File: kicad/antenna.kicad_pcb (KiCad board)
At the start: 2 copper layers, 84.1 x 61.7 mm, 37 parts, among them J1 Bus_PCI_Express_x1, J4 Conn_01x02, J5 Conn_02x08_Odd_Even, J6 USB_C_Receptacle_USB2.0_16P, U2 RP2040, U4 W25Q128JVP, U9 MCP25625T-E/ML, X1 ABM8-272-T3, Y2 X322516MLB4SI

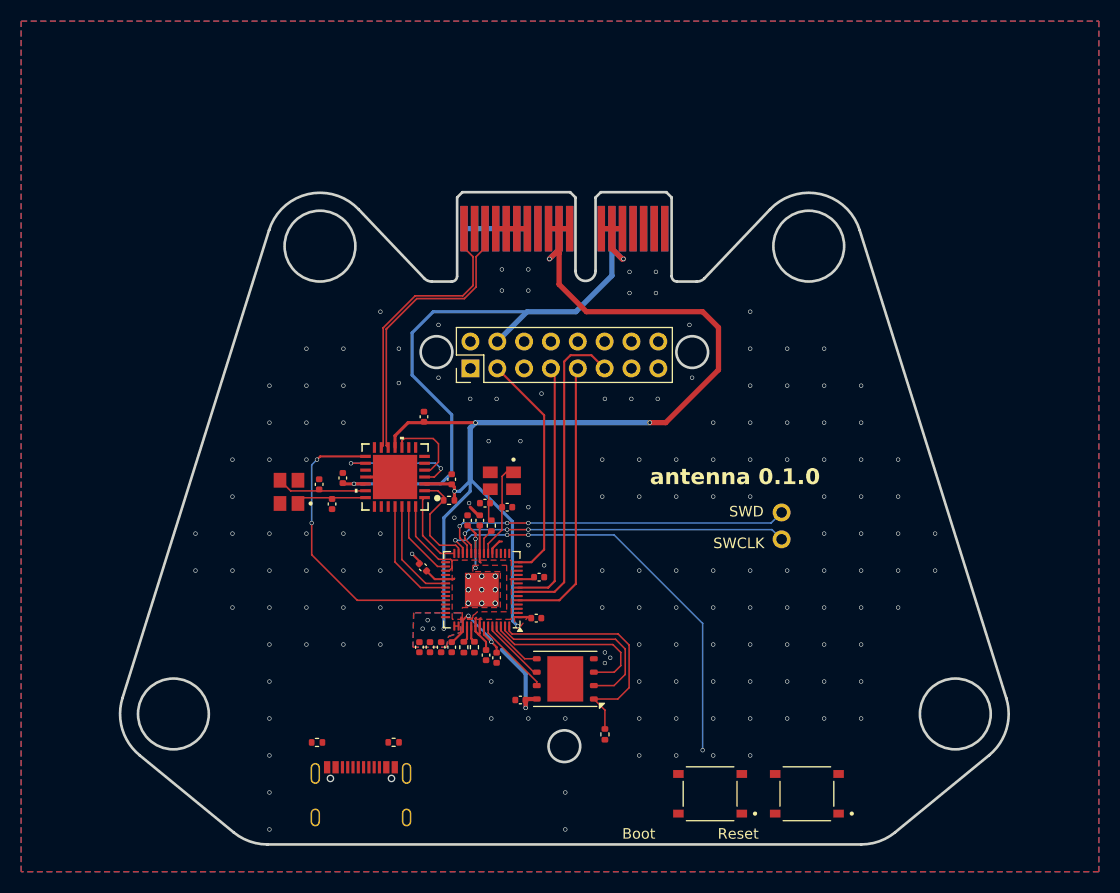
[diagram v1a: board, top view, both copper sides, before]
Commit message: create RFD900 footprint, update schematic library to global
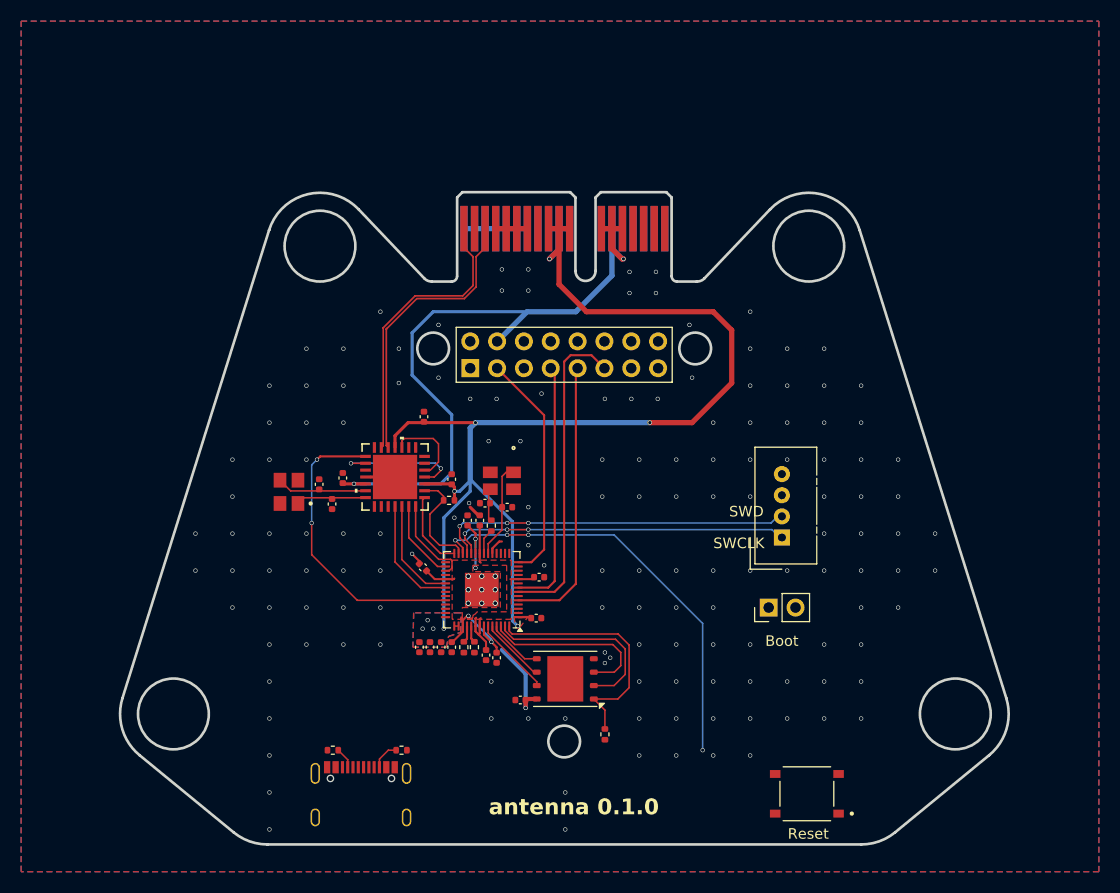
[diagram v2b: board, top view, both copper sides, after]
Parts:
- removed J4: Conn_01x02, Connector_PinHeader_2.54mm:PinHeader_1x02_P2.54mm_Vertical
- removed S1: TS-1187A-B-A-B, TS-1187A-B-A-B:SW_TS-1187A-B-A-B
- added J2: Conn_01x04, Connector:NS-Tech_Grove_1x04_P2mm_Vertical, F.Cu at (167.0, 93.4)
- added U1: RFD900, 4in-antenna:RFD900, F.Cu at (146.4, 76.1)
- J5: value Conn_02x08_Odd_Even -> Conn_01x02; footprint Connector_PinSocket_2.54mm:PinSocket_2x08_P2.54mm_Vertical -> Connector_PinHeader_2.54mm:PinHeader_1x02_P2.54mm_Vertical
- S2: footprint TS-1187A-B-A-B:SW_TS-1187A-B-A-B -> 4in-kicad-library:TS-1187A-B-A-B
- U9: footprint MCP25625T_E_ML:QFN28_6X6MC_MCH -> 4in-kicad-library:QFN28_6X6MC_MCH
- X1: value ABM8-272-T3 -> RP2040 Crystal; footprint ABM8-272-T3:ABM8-272-T3_ABR -> 4in-kicad-library:ABM8-272-T3_ABR
- Y2: footprint X322516MLB4SI:OSC_X322516MLB4SI -> 4in-kicad-library:X322516MLB4SI
- moved J5 30.7 mm to (165.8, 100.0)
- moved R4 1.67 mm to (124.5, 113.5)
- moved R3 1.05 mm to (131.0, 113.5)
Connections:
- J5 pad 1: GND -> /~{USB_BOOT_S}
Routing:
- net +3.3V: track 137.4 -> 140.5 mm
- net Net-(J6-CC2): track 0.00 -> 2.70 mm
- net Net-(J6-CC1): track 0.00 -> 1.99 mm
- net GND: vias 163 -> 159
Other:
- outline, holes or cut-outs redrawn

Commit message: route USB, add LED
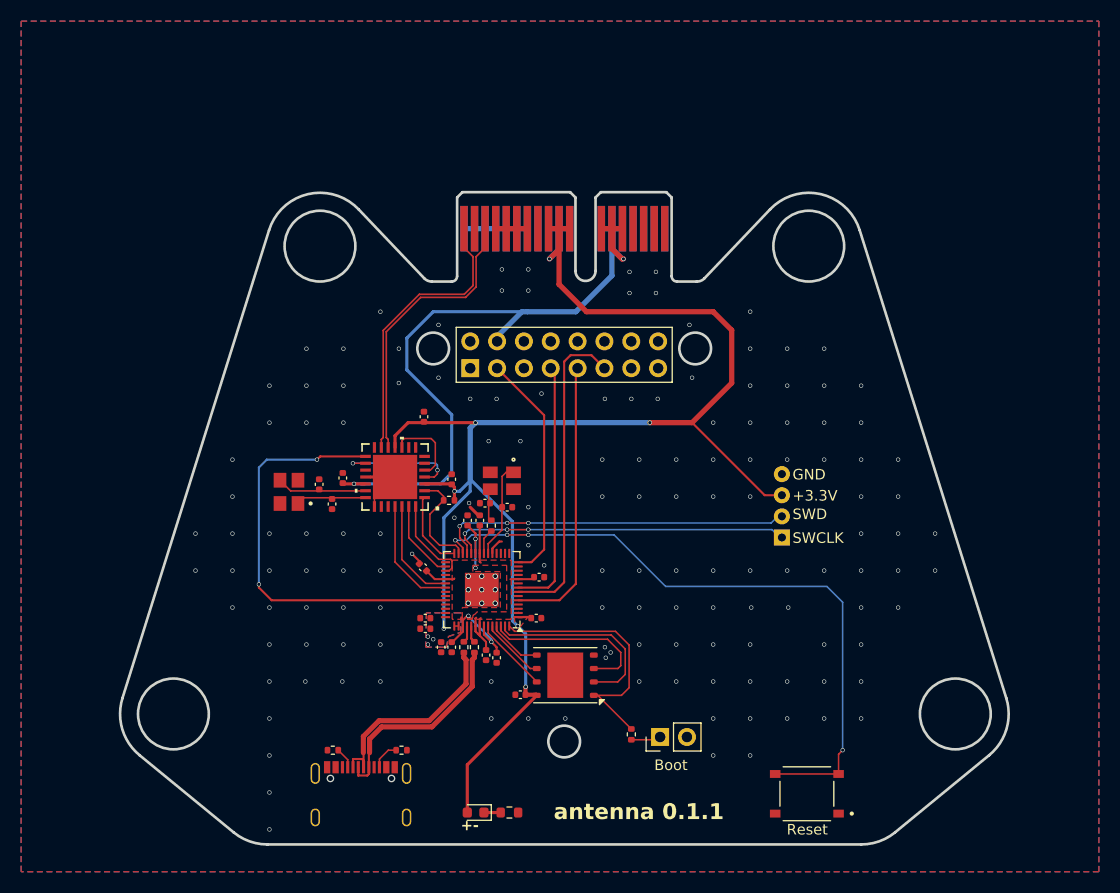
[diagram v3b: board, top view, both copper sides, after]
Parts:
- added D1: LED, LED_SMD:LED_0603_1608Metric, F.Cu at (138.0, 119.4)
- added R1: 1.5k, Resistor_SMD:R_0603_1608Metric, F.Cu at (141.2, 119.4)
- moved J5 16.0 mm to (155.5, 112.2)
- moved C215 2.81 mm to (133.2, 101.0), turned to 180 degrees
- moved R30 2.50 mm to (152.8, 112.0)
- moved C216 1.81 mm to (133.2, 102.0), turned to 180 degrees
- moved C40 0.50 mm to (142.2, 108.2)
- moved U4 0.34 mm to (146.5, 106.4)
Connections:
- U1 pad 5: Vusb -> unconnected-(U1-Vusb-Pad5)
- U1 pad 6: Vusb -> unconnected-(U1-Vusb-Pad6)
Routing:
- net +3.3V: track 140.5 -> 165.3 mm
- net /RUN: track 40.6 -> 63.5 mm
- net USB_D+: track 0.00 -> 20.2 mm
- net USB_D-: track 0.00 -> 20.2 mm
- net CANSTBY: track 28.4 -> 40.0 mm
- net GND: track 16.3 -> 19.9 mm, vias 159 -> 154
- net /~{USB_BOOT_S}: track 0.00 -> 2.83 mm
- net Net-(D1-K): track 0.00 -> 1.59 mm
- net /QSPI_SS: track 23.5 -> 24.6 mm
- net +5V: track 66.7 -> 67.4 mm
- net tx: track 12.1 -> 11.5 mm
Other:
- board text added: "+-"
- board text added: "+3.3V"
- board text added: "."
- board text added: "0.1.1"
- board text added: "GND"
- board text added: "antenna"
- board text added: "antenna 0.1.1"
- board text removed: "antenna 0.1.0"

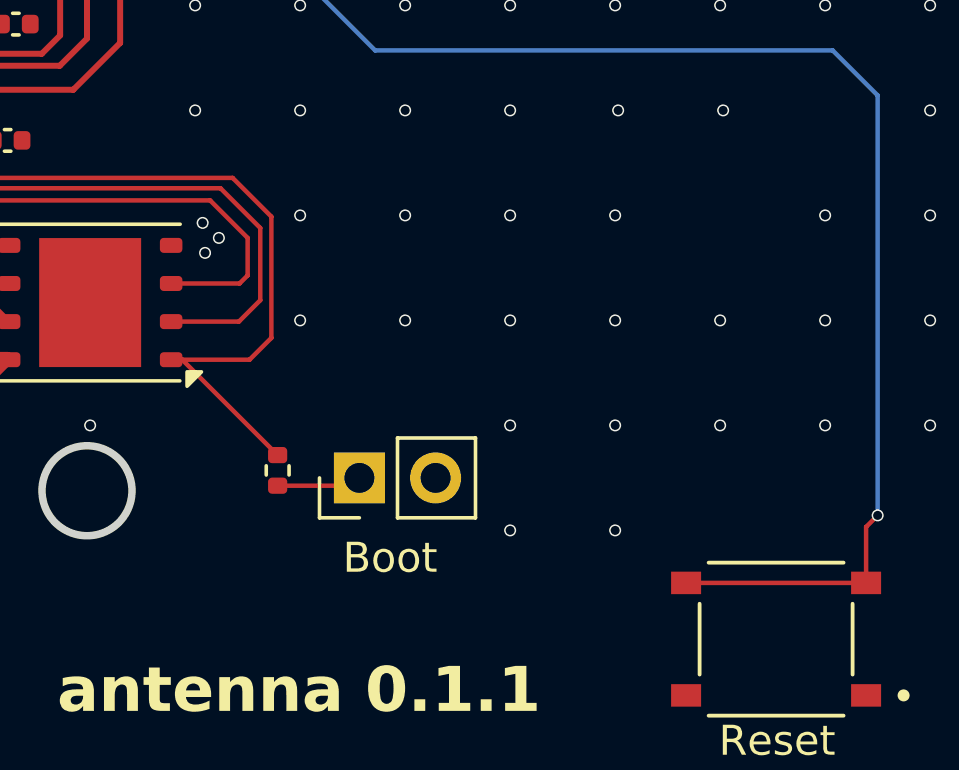
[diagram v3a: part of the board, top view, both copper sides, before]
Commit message: add new DXF of the rack
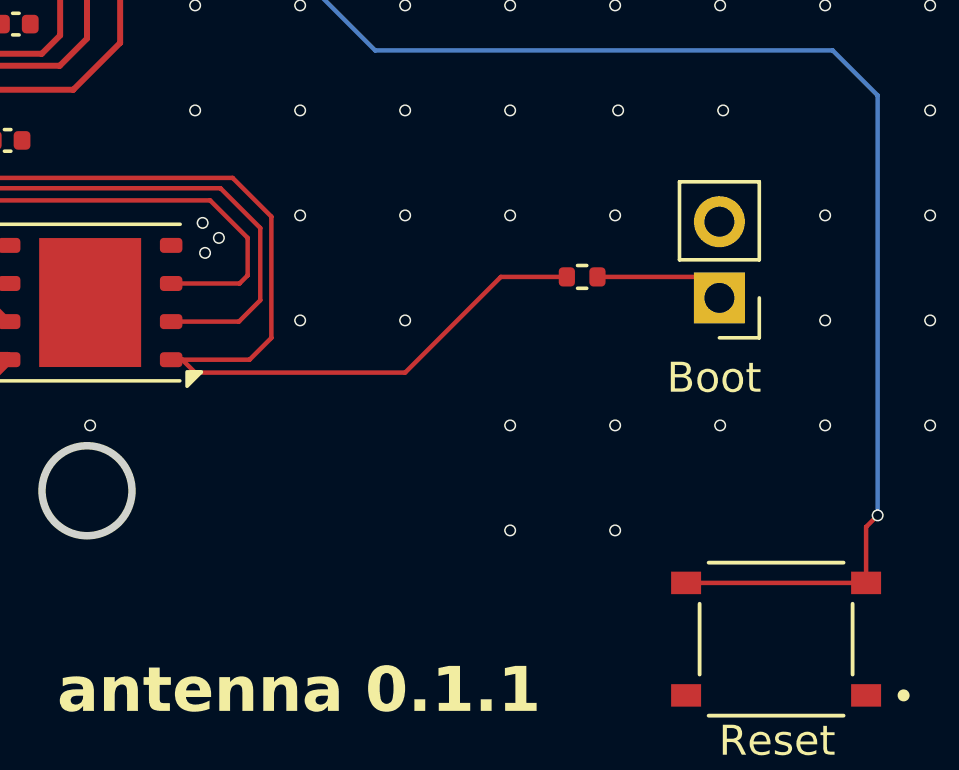
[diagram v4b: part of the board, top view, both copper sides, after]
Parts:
- moved J5 13.4 mm to (167.5, 106.2), turned to 180 degrees
- moved R30 12.0 mm to (162.9, 105.5), turned to 0 degrees
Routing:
- net /QSPI_SS: track 24.6 -> 34.5 mm
- net /~{USB_BOOT_S}: track 2.83 -> 4.35 mm
- net GND: vias 154 -> 151

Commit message: finalize version 0.1.1 for ordering
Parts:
- moved R4 1.26 mm to (123.3, 113.1)
- moved R3 0.40 mm to (131.0, 113.1)
- moved C213 0.20 mm to (144.2, 97.1)
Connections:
- net CTS renamed CTS_rfd
- U1 pad 10: P3.3 -> unconnected-(U1-P2.2-Pad10)
- U1 pad 11: RTS -> RTS_rfd
- U1 pad 12: P1.3 -> unconnected-(U1-P2.1-Pad12)
- U1 pad 13: P1.0 -> unconnected-(U1-P0.1-Pad13)
- U1 pad 14: P1.2 -> unconnected-(U1-P2.0-Pad14)
- U1 pad 15: P1.1 -> unconnected-(U1-P2.6-Pad15)
- U1 pad 7: RX -> RX_rfd
- U1 pad 8: P3.4 -> unconnected-(U1-P2.3-Pad8)
- U1 pad 9: TX -> TX_rfd
- U2 pad 11: unconnected-(U2-GPIO8-Pad11) -> RX_rfd
- U2 pad 5: TX -> unconnected-(U2-GPIO3-Pad5)
- U2 pad 7: RTS -> TX_rfd
- U2 pad 8: RX -> RTS_rfd
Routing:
- net RTS: track 30.6 -> 0.00 mm
- net RTS_rfd: track 0.00 -> 30.0 mm
- net TX: track 26.9 -> 0.00 mm
- net TX_rfd: track 0.00 -> 26.1 mm
- net RX: track 24.8 -> 0.00 mm
- net RX_rfd: track 0.00 -> 21.5 mm
- net Net-(J6-CC1): track 1.99 -> 3.35 mm
- net +5V: track 67.4 -> 68.1 mm
- net +3.3V: track 165.3 -> 165.9 mm
- net GND: vias 151 -> 168

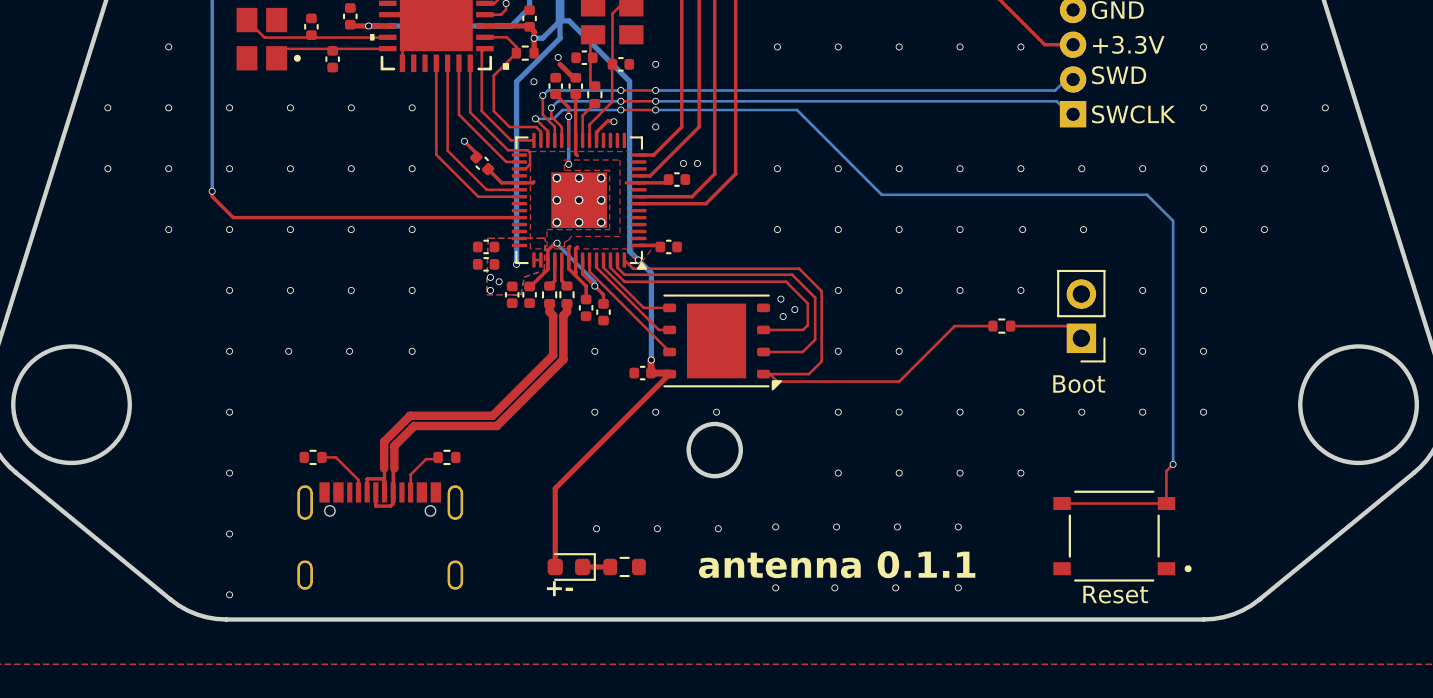
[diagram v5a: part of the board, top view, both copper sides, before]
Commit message: move flash away from mounting hole, update to text to 0.2.0
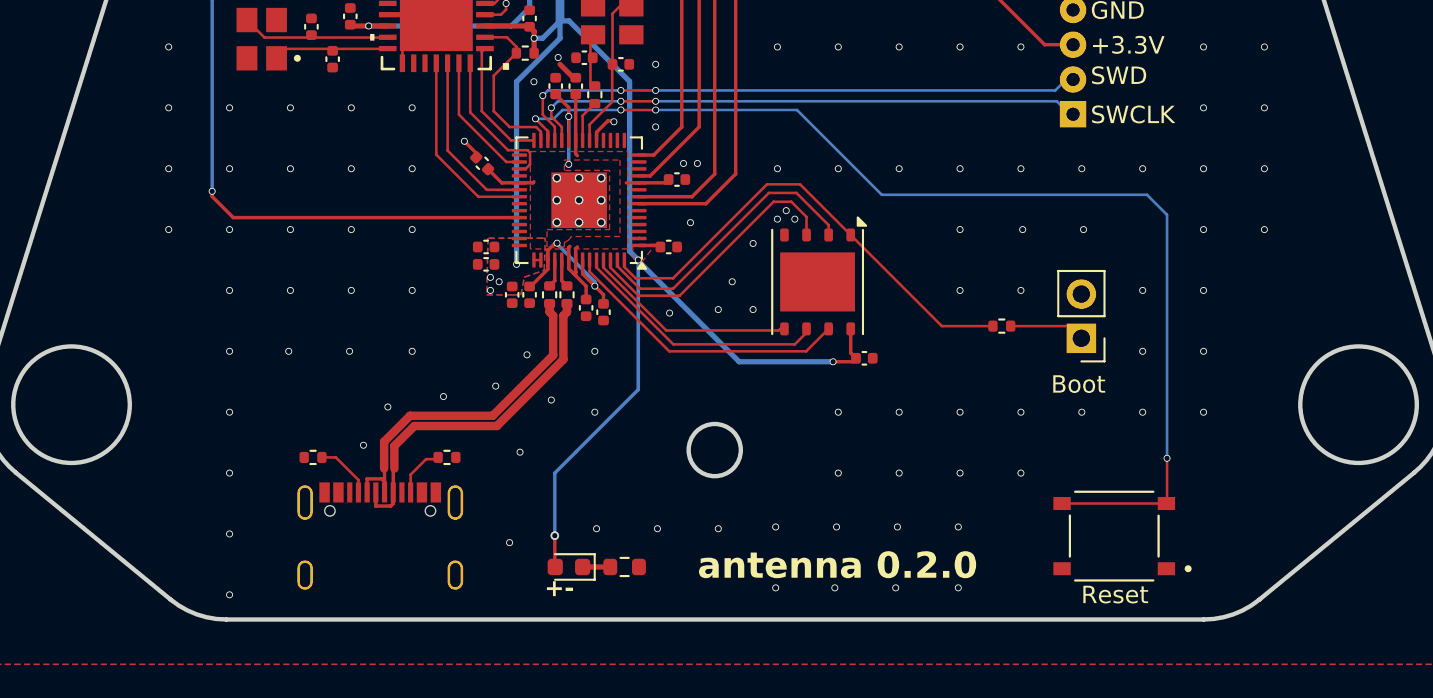
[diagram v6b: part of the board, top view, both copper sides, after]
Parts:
- moved C40 12.8 mm to (155.0, 107.4), turned to 0 degrees
- moved U4 6.73 mm to (152.3, 103.0), turned to -90 degrees
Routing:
- net +3.3V: track 165.9 -> 180.7 mm, vias 10 -> 11
- net /QSPI_SD3: track 7.18 -> 16.8 mm
- net /QSPI_SCLK: track 6.12 -> 14.8 mm
- net /QSPI_SD0: track 4.85 -> 12.4 mm
- net /QSPI_SS: track 34.5 -> 27.5 mm
- net /QSPI_SD1: track 17.9 -> 16.7 mm
- net /QSPI_SD2: track 16.6 -> 16.0 mm
- net GND: vias 168 -> 169
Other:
- board text added: "antenna 0.2.0"
- board text removed: "antenna 0.1.1"

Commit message: export final production files for 0.2.0
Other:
- board text added: "0.2.0"
- board text removed: "0.1.1"
